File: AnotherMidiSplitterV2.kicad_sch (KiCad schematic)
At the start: 40 parts, among them J1 IN, J10 OUT, J11 OUT, J2 USB_power, J4 OUT, J5 OUT, J6 OUT, J7 OUT, J8 OUT, J9 OUT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

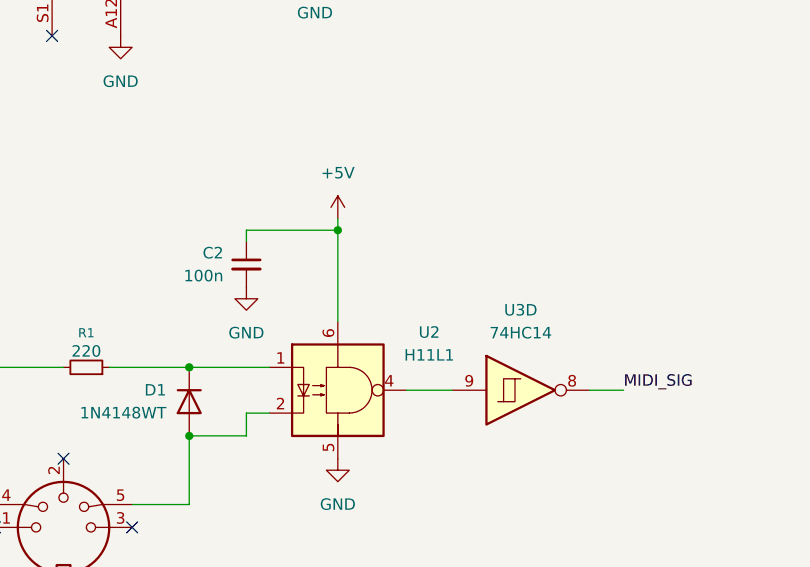
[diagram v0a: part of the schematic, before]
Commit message: add resistor to optoisolator
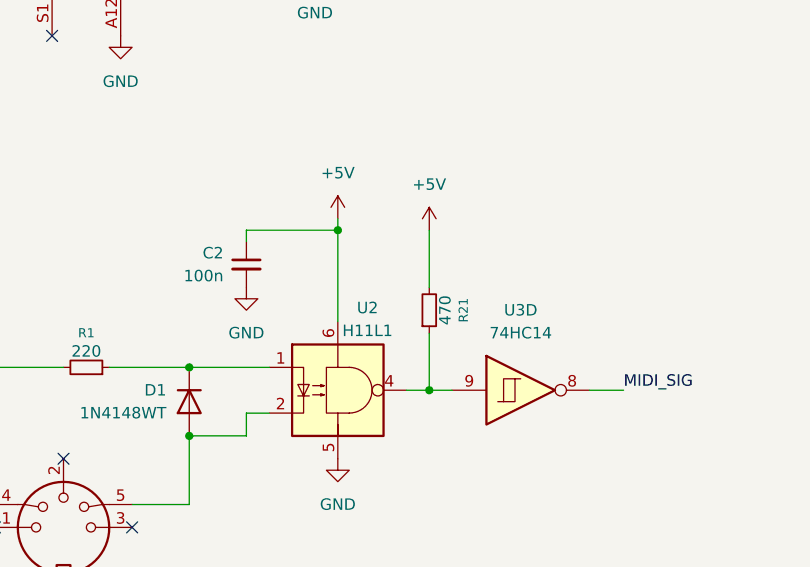
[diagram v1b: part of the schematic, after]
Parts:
- added R21: 470, Resistor_SMD:R_0603_1608Metric_Pad0.98x0.95mm_HandSolder, symbol Device:R_Small
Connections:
- net +5V: now also R21.2
- net at U2.4, U3.9: now also R21.1
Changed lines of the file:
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@@
 	)
 	(junction
+		(at 73.66 105.41)
+		(diameter 0)
+		(color 0 0 0 0)
+	)
+	(junction
 		(at 46.99 102.87)
 		(diameter 0)
@@
 	(wire
 		(pts
+			(xy 73.66 87.63) (xy 73.66 93.98)
+		)
+		(stroke
+			(width 0)
+			(type default)
+		)
+	)
+	(wire
+		(pts
 			(xy 242.57 72.39) (xy 243.84 72.39)
 		)
@@
 	(wire
 		(pts
+			(xy 73.66 99.06) (xy 73.66 105.41)
+		)
+		(stroke
+			(width 0)
+			(type default)
+		)
+	)
+	(wire
+		(pts
 			(xy 71.12 40.64) (xy 71.12 41.91)
 		)
@@
 	(wire
 		(pts
-			(xy 71.12 105.41) (xy 76.2 105.41)
+			(xy 71.12 105.41) (xy 73.66 105.41)
 		)
 		(stroke
@@
 	(wire
 		(pts
+			(xy 73.66 105.41) (xy 76.2 105.41)
+		)
+		(stroke
+			(width 0)
+			(type default)
+		)
+	)
+	(wire
+		(pts
 			(xy 111.76 49.53) (xy 111.76 50.8)
 		)
@@
 	)
 	(symbol
+		(lib_id "Device:R_Small")
+		(at 73.66 96.52 0)
+		(mirror x)
+		(unit 1)
+		(exclude_from_sim no)
+		(in_bom yes)
+		(on_board yes)
+		(dnp no)
+		(property "Reference" "R21"
+			(at 77.47 96.52 90)
+			(effects
+				(font
+					(size 1.016 1.016)
+				)
+			)
+		)
+		(property "Value" "470"
+			(at 75.438 96.52 90)
+			(effects
+				(font
+					(size 1.27 1.27)
+				)
+			)
+		)
+		(property "Footprint" "Resistor_SMD:R_0603_1608Metric_Pad0.98x0.95mm_HandSolder"
+			(at 73.66 96.52 0)
+			(effects
+				(font
+					(size 1.27 1.27)
+				)
+				(hide yes)
+			)
+		)
+		(property "Datasheet" "~"
+			(at 73.66 96.52 0)
+			(effects
+				(font
+					(size 1.27 1.27)
+				)
+				(hide yes)
+			)
+		)
+		(property "Description" "Resistor, small symbol"
+			(at 73.66 96.52 0)
+			(effects
+				(font
+					(size 1.27 1.27)
+				)
+				(hide yes)
+			)
+		)
+		(pin "1"
+		)
+		(pin "2"
+		)
+		(instances
+			(project "AnotherMidiSplitterV2"
+				(path "/c84a968a-2048-42bb-b985-8c3fe6c218ef"
+					(reference "R21")
+					(unit 1)
+				)
+			)
+		)
+	)
+	(symbol
 		(lib_id "power:GND")
 		(at 39.37 66.04 0)
@@
 	)
 	(symbol
+		(lib_id "power:+5V")
+		(at 73.66 87.63 0)
+		(unit 1)
+		(exclude_from_sim no)
+		(in_bom yes)
+		(on_board yes)
+		(dnp no)
+		(fields_autoplaced yes)
+		(property "Reference" "#PWR032"
+			(at 73.66 91.44 0)
+			(effects
+				(font
+					(size 1.27 1.27)
+				)
+				(hide yes)
+			)
+		)
+		(property "Value" "+5V"
+			(at 73.66 82.55 0)
+			(effects
+				(font
+					(size 1.27 1.27)
+				)
+			)
+		)
+		(property "Footprint" ""
+			(at 73.66 87.63 0)
+			(effects
+				(font
+					(size 1.27 1.27)
+				)
+				(hide yes)
+			)
+		)
+		(property "Datasheet" ""
+			(at 73.66 87.63 0)
+			(effects
+				(font
+					(size 1.27 1.27)
+				)
+				(hide yes)
+			)
+		)
+		(property "Description" "Power symbol creates a global label with name \"+5V\""
+			(at 73.66 87.63 0)
+			(effects
+				(font
+					(size 1.27 1.27)
+				)
+				(hide yes)
+			)
+		)
+		(pin "1"
+		)
+		(instances
+			(project "AnotherMidiSplitterV2"
+				(path "/c84a968a-2048-42bb-b985-8c3fe6c218ef"
+					(reference "#PWR032")
+					(unit 1)
+				)
+			)
+		)
+	)
+	(symbol
 		(lib_id "74xx:74HC14")
 		(at 173.99 72.39 0)
@@
 		(on_board yes)
 		(dnp no)
-		(fields_autoplaced yes)
 		(property "Reference" "U2"
-			(at 73.66 98.9898 0)
+			(at 66.802 96.266 0)
 			(effects
 				(font
@@
 		)
 		(property "Value" "H11L1"
-			(at 73.66 101.5298 0)
+			(at 66.802 98.806 0)
 			(effects
 				(font

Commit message: add logo and some descriptions to schematic, update gitignore
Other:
- note added: "INPUT"
- note added: "OUTPUTS"
- note added: "POWER"
- company: (none) -> Miłosz Derżko
- title: (none) -> AnotherMidiSplitterV2
- moved on the sheet: C1, C2, C3, C4, C5, D1, D2, J1, J2, R1, R2, R21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

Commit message: Update Variables
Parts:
- added D3: PWR LED, LED_SMD:LED_1206_3216Metric, symbol Device:LED
- added D4: PWR LED, LED_THT:LED_D3.0mm_Horizontal_O1.27mm_Z2.0mm, symbol Device:LED
- added R22, R23: 470, Resistor_SMD:R_0603_1608Metric_Pad0.98x0.95mm_HandSolder, symbol Device:R_Small
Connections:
- net +5V: now also D3.2 (A), D4.2 (A)
- net GND: now also R22.2, R23.2
- net at R19.2: now also J10.4; no longer J10.5
- net at R14.1: now also J9.5; no longer J9.4
- net at R16.1: now also J11.5; no longer J11.4
- net at R18.2: now also J9.4; no longer J9.5
- net at J5.4: now also R10.2; no longer R6.1
- net at J5.5: now also R6.1; no longer R10.2
- net at R13.1: now also J8.5; no longer J8.4
- net at R17.2: now also J8.4; no longer J8.5
- net at R9.2: now also J4.4; no longer J4.5
- net at R5.1: now also J4.5; no longer J4.4
- net at R12.2: now also J7.4; no longer J7.5
- net at J6.4: now also R11.2; no longer R7.1
- net at J6.5: now also R7.1; no longer R11.2
- net at R15.1: now also J10.5; no longer J10.4
- net at R8.1: now also J7.5; no longer J7.4
- net at R20.2: now also J11.4; no longer J11.5
- new net: D3.1 (K), R22.1
- new net: D4.1 (K), R23.1
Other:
- note added: "Choose one"
- company: Miłosz Derżko -> ${Company}
- title: AnotherMidiSplitterV2 -> ${ProjectTitle}
- moved on the sheet: D2, J10, J11, J4, J5, J6, J7, J8, J9, R4
